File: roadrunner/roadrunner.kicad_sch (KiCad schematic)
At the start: 48 parts, among them J1 Battery_conn, J2 battery_conn_r, SW1 SW_Push, SW10 SW_Push, SW10_r1 SW_Push, SW11 SW_Push, SW11_r1 SW_Push, SW12 SW_Push, SW12_r1 SW_Push, SW13 SW_Push, SW13_r1 SW_Push, SW14 SW_Push, SW14_r1 SW_Push, SW15 SW_Push, SW15_r1 SW_Push, SW16 SW_Push, SW16_r1 SW_Push, SW17 SW_Push, SW17_r1 SW_Push, SW1_r1 SW_Push, SW2 SW_Push, SW2_r1 SW_Push, SW3 SW_Push, SW3_r1 SW_Push, SW4 SW_Push, SW4_r1 SW_Push, SW5 SW_Push, SW5_r1 SW_Push, SW6 SW_Push, SW6_r1 SW_Push, SW7 SW_Push, SW7_r1 SW_Push, SW8 SW_Push, SW8_r1 SW_Push, SW9 SW_Push, SW9_r1 SW_Push, U1 ProMicro-kbd, U2 ProMicro-kbd

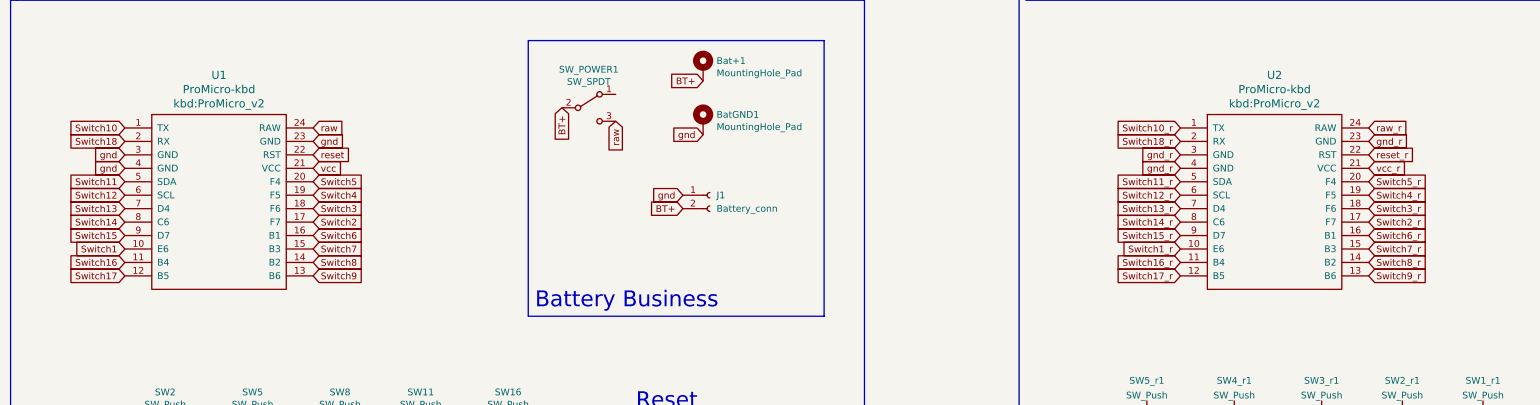
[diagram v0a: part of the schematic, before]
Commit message: update schematic
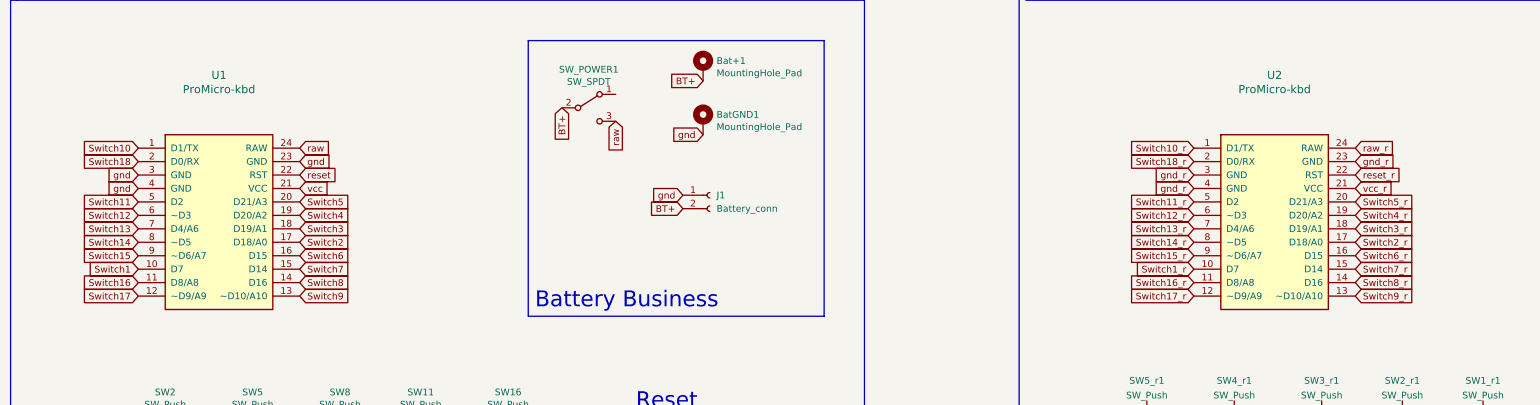
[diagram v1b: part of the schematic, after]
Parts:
- U1, U2: footprint kbd:ProMicro_v2 -> Arduino:Sparkfun_Pro_Micro; symbol sweepv2-rescue:ProMicro-kbd-bigblackpill-34key-rescue -> Arduino:Sparkfun_Pro_Micro

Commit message: update shape
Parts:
- TRRS1, TRRS2: footprint (none) -> Connector_Audio:Jack_3.5mm_PJ320E_Horizontal
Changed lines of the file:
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@@
   (symbol (lib_id "Connector:AudioJack4") (at 331.47 133.35 0) (unit 1)
     (in_bom yes) (on_board yes) (fields_autoplaced)
-    (property "Reference" "TRRS2" (id 0) (at 328.93 125.5735 0))
-    (property "Value" "AudioJack4" (id 1) (at 328.93 128.3486 0))
-    (property "Footprint" "" (id 2) (at 331.47 133.35 0)
+    (property "Reference" "TRRS2" (id 0) (at 328.93 124.46 0))
+    (property "Value" "AudioJack4" (id 1) (at 328.93 127 0))
+    (property "Footprint" "Connector_Audio:Jack_3.5mm_PJ320E_Horizontal" (id 2) (at 331.47 133.35 0)
       (effects (font (size 1.27 1.27)) hide)
     )
@@
   (symbol (lib_id "Connector:AudioJack4") (at 135.89 129.54 0) (unit 1)
     (in_bom yes) (on_board yes) (fields_autoplaced)
-    (property "Reference" "TRRS1" (id 0) (at 133.35 121.7635 0))
-    (property "Value" "AudioJack4" (id 1) (at 133.35 124.5386 0))
-    (property "Footprint" "" (id 2) (at 135.89 129.54 0)
+    (property "Reference" "TRRS1" (id 0) (at 133.35 120.65 0))
+    (property "Value" "AudioJack4" (id 1) (at 133.35 123.19 0))
+    (property "Footprint" "Connector_Audio:Jack_3.5mm_PJ320E_Horizontal" (id 2) (at 135.89 129.54 0)
       (effects (font (size 1.27 1.27)) hide)
     )
@@
   )
   (symbol (lib_id "Switch:SW_SPDT") (at 121.92 34.29 0) (unit 1)
-    (in_bom yes) (on_board yes)
-    (property "Reference" "SW_POWER1" (id 0) (at 121.92 27.051 0))
-    (property "Value" "SW_SPDT" (id 1) (at 121.92 29.3624 0))
+    (in_bom yes) (on_board yes) (fields_autoplaced)
+    (property "Reference" "SW_POWER1" (id 0) (at 121.92 26.67 0))
+    (property "Value" "SW_SPDT" (id 1) (at 121.92 29.21 0))
     (property "Footprint" "battery_switch:SPDT_C128955" (id 2) (at 121.92 34.29 0)
       (effects (font (size 1.27 1.27)) hide)
@@
   )
   (symbol (lib_id "Switch:SW_SPDT") (at 317.5 31.75 0) (unit 1)
-    (in_bom yes) (on_board yes)
-    (property "Reference" "SW_POWERR1" (id 0) (at 317.5 24.511 0))
-    (property "Value" "SW_SPDT" (id 1) (at 317.5 26.8224 0))
+    (in_bom yes) (on_board yes) (fields_autoplaced)
+    (property "Reference" "SW_POWERR1" (id 0) (at 317.5 24.13 0))
+    (property "Value" "SW_SPDT" (id 1) (at 317.5 26.67 0))
     (property "Footprint" "battery_switch:SPDT_C128955" (id 2) (at 317.5 31.75 0)
       (effects (font (size 1.27 1.27)) hide)
@@
     )
     (path "/5707fb00-48c3-46d9-8f62-42ff2e9ad9f5"
-      (reference "TRRS1") (unit 1) (value "AudioJack4") (footprint "")
+      (reference "TRRS1") (unit 1) (value "AudioJack4") (footprint "Connector_Audio:Jack_3.5mm_PJ320E_Horizontal")
     )
     (path "/5340d998-a6ef-44fa-806e-718c814691ee"
-      (reference "TRRS2") (unit 1) (value "AudioJack4") (footprint "")
+      (reference "TRRS2") (unit 1) (value "AudioJack4") (footprint "Connector_Audio:Jack_3.5mm_PJ320E_Horizontal")
     )
     (path "/6801880a-11a2-4a6a-9688-e81ed1f59985"

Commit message: basic v2 designs
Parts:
- removed TRRS1, TRRS2: AudioJack4, Connector_Audio:Jack_3.5mm_PJ320E_Horizontal, symbol Connector:AudioJack4
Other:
- note removed: "Useless TRRS"
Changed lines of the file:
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@@
-    (effects (font (size 2.9972 2.9972)) (justify left bottom))
-  )
-  (text "Useless TRRS\n" (at 321.31 121.92 0)
     (effects (font (size 2.9972 2.9972)) (justify left bottom))
   )
@@
     (effects (font (size 2.9972 2.9972)) (justify left bottom))
   )
-  (text "Useless TRRS\n" (at 123.19 118.11 0)
-    (effects (font (size 2.9972 2.9972)) (justify left bottom))
-  )
   (text "Battery Business" (at 308.61 74.93 0)
     (effects (font (size 2.9972 2.9972)) (justify left bottom))
@@
     )
   )
-  (global_label "vcc_r" (shape input) (at 336.55 133.35 0) (fields_autoplaced)
-    (effects (font (size 1.27 1.27)) (justify left))
-    (property "Intersheet References" "${INTERSHEET_REFS}" (id 0) (at 343.7728 133.2706 0)
-      (effects (font (size 1.27 1.27)) (justify left) hide)
-    )
-  )
   (global_label "gnd" (shape input) (at 80.01 95.25 270) (fields_autoplaced)
     (effects (font (size 1.27 1.27)) (justify right))
     (property "Intersheet References" "${INTERSHEET_REFS}" (id 0) (at 13.97 66.04 0)
-      (effects (font (size 1.27 1.27)) hide)
-    )
-  )
-  (global_label "gnd" (shape input) (at 140.97 134.62 0) (fields_autoplaced)
-    (effects (font (size 1.27 1.27)) (justify left))
-    (property "Intersheet References" "${INTERSHEET_REFS}" (id 0) (at 13.97 67.31 0)
       (effects (font (size 1.27 1.27)) hide)
     )
@@
     )
   )
-  (global_label "gnd" (shape input) (at 140.97 127 0) (fields_autoplaced)
-    (effects (font (size 1.27 1.27)) (justify left))
-    (property "Intersheet References" "${INTERSHEET_REFS}" (id 0) (at 13.97 59.69 0)
-      (effects (font (size 1.27 1.27)) hide)
-    )
-  )
   (global_label "Switch5" (shape input) (at 101.6 95.25 270) (fields_autoplaced)
     (effects (font (size 1.27 1.27)) (justify right))
@@
     (property "Intersheet References" "${INTERSHEET_REFS}" (id 0) (at 13.97 66.04 0)
       (effects (font (size 1.27 1.27)) hide)
-    )
-  )
-  (global_label "gnd_r" (shape input) (at 336.55 130.81 0) (fields_autoplaced)
-    (effects (font (size 1.27 1.27)) (justify left))
-    (property "Intersheet References" "${INTERSHEET_REFS}" (id 0) (at 344.0752 130.8894 0)
-      (effects (font (size 1.27 1.27)) (justify left) hide)
     )
   )
@@
     )
   )
-  (global_label "gnd_r" (shape input) (at 336.55 138.43 0) (fields_autoplaced)
-    (effects (font (size 1.27 1.27)) (justify left))
-    (property "Intersheet References" "${INTERSHEET_REFS}" (id 0) (at 344.0752 138.5094 0)
-      (effects (font (size 1.27 1.27)) (justify left) hide)
-    )
-  )
   (global_label "raw" (shape input) (at 127 36.83 270) (fields_autoplaced)
     (effects (font (size 1.27 1.27)) (justify right))
@@
     )
   )
-  (global_label "Switch18" (shape input) (at 140.97 132.08 0) (fields_autoplaced)
-    (effects (font (size 1.27 1.27)) (justify left))
-    (property "Intersheet References" "${INTERSHEET_REFS}" (id 0) (at 13.97 67.31 0)
-      (effects (font (size 1.27 1.27)) hide)
-    )
-  )
   (global_label "reset_r" (shape input) (at 336.55 110.49 0) (fields_autoplaced)
     (effects (font (size 1.27 1.27)) (justify left))
@@
     )
   )
-  (global_label "vcc" (shape input) (at 140.97 129.54 0) (fields_autoplaced)
-    (effects (font (size 1.27 1.27)) (justify left))
-    (property "Intersheet References" "${INTERSHEET_REFS}" (id 0) (at 13.97 59.69 0)
-      (effects (font (size 1.27 1.27)) hide)
-    )
-  )
   (global_label "gnd_r" (shape input) (at 265.43 92.71 270) (fields_autoplaced)
     (effects (font (size 1.27 1.27)) (justify right))
@@
     (property "Intersheet References" "${INTERSHEET_REFS}" (id 0) (at 285.6706 104.1056 90)
       (effects (font (size 1.27 1.27)) (justify right) hide)
-    )
-  )
-  (global_label "Switch18_r" (shape input) (at 336.55 135.89 0) (fields_autoplaced)
-    (effects (font (size 1.27 1.27)) (justify left))
-    (property "Intersheet References" "${INTERSHEET_REFS}" (id 0) (at 208.28 -27.94 0)
-      (effects (font (size 1.27 1.27)) hide)
     )
   )
@@
     (pin "2")
   )
-  (symbol (lib_id "Connector:AudioJack4") (at 331.47 133.35 0) (unit 1)
-    (in_bom yes) (on_board yes) (fields_autoplaced)
-    (property "Reference" "TRRS2" (id 0) (at 328.93 124.46 0))
-    (property "Value" "AudioJack4" (id 1) (at 328.93 127 0))
-    (property "Footprint" "Connector_Audio:Jack_3.5mm_PJ320E_Horizontal" (id 2) (at 331.47 133.35 0)
-      (effects (font (size 1.27 1.27)) hide)
-    )
-    (property "Datasheet" "~" (id 3) (at 331.47 133.35 0)
-      (effects (font (size 1.27 1.27)) hide)
-    )
-    (pin "R1")
-    (pin "R2")
-    (pin "S")
-    (pin "T")
-  )
-  (symbol (lib_id "Connector:AudioJack4") (at 135.89 129.54 0) (unit 1)
-    (in_bom yes) (on_board yes) (fields_autoplaced)
-    (property "Reference" "TRRS1" (id 0) (at 133.35 120.65 0))
-    (property "Value" "AudioJack4" (id 1) (at 133.35 123.19 0))
-    (property "Footprint" "Connector_Audio:Jack_3.5mm_PJ320E_Horizontal" (id 2) (at 135.89 129.54 0)
-      (effects (font (size 1.27 1.27)) hide)
-    )
-    (property "Datasheet" "~" (id 3) (at 135.89 129.54 0)
-      (effects (font (size 1.27 1.27)) hide)
-    )
-    (pin "R1")
-    (pin "R2")
-    (pin "S")
-    (pin "T")
-  )
   (symbol (lib_id "Connector:Conn_01x02_Female") (at 332.74 49.53 0) (unit 1)
     (in_bom yes) (on_board yes) (fields_autoplaced)
@@
       (reference "SW_POWERR1") (unit 1) (value "SW_SPDT") (footprint "battery_switch:SPDT_C128955")
     )
-    (path "/5707fb00-48c3-46d9-8f62-42ff2e9ad9f5"
-      (reference "TRRS1") (unit 1) (value "AudioJack4") (footprint "Connector_Audio:Jack_3.5mm_PJ320E_Horizontal")
-    )
-    (path "/5340d998-a6ef-44fa-806e-718c814691ee"
-      (reference "TRRS2") (unit 1) (value "AudioJack4") (footprint "Connector_Audio:Jack_3.5mm_PJ320E_Horizontal")
-    )
     (path "/6801880a-11a2-4a6a-9688-e81ed1f59985"

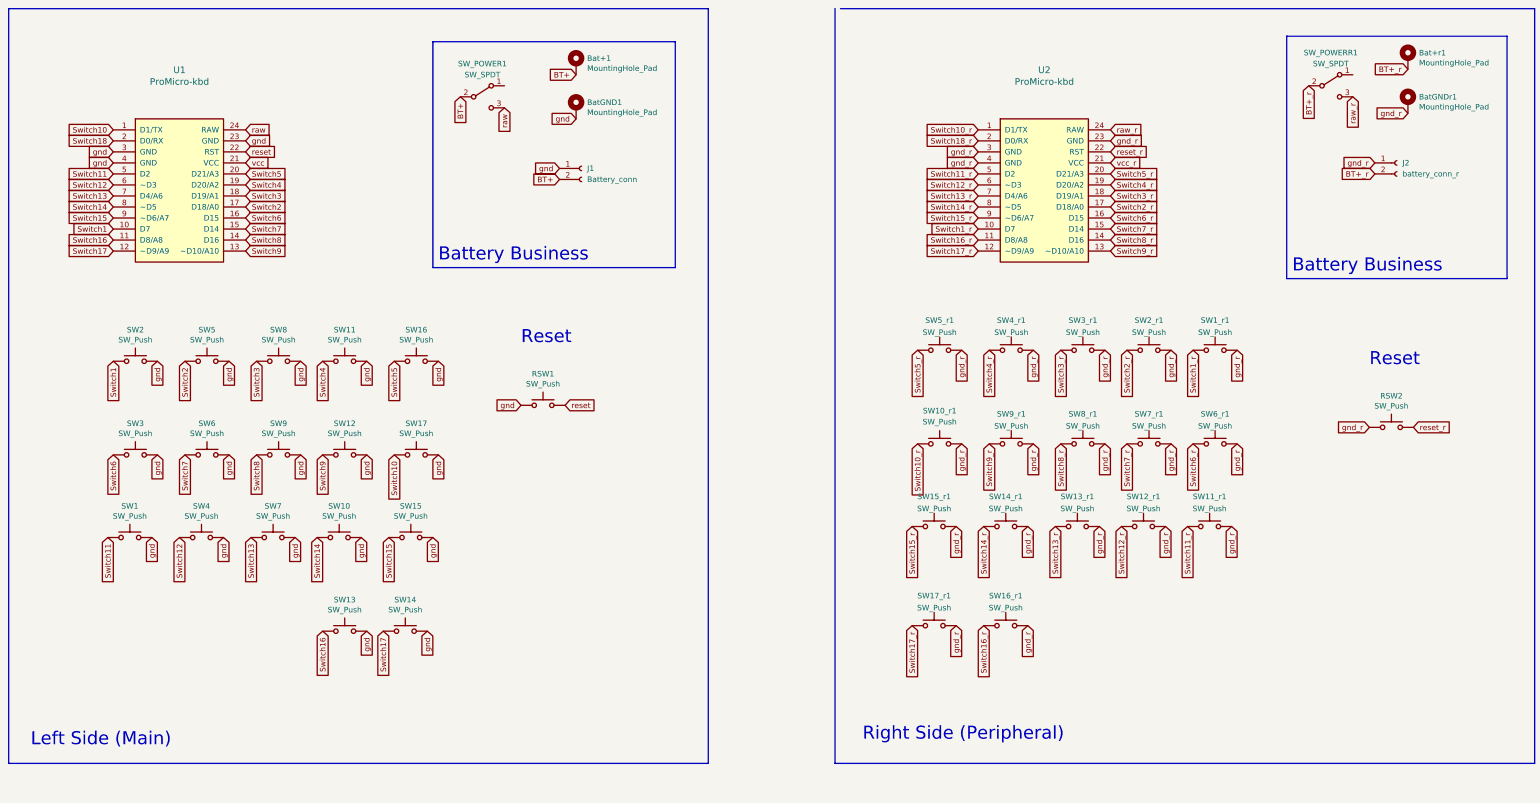
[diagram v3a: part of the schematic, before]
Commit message: begin adding diodes
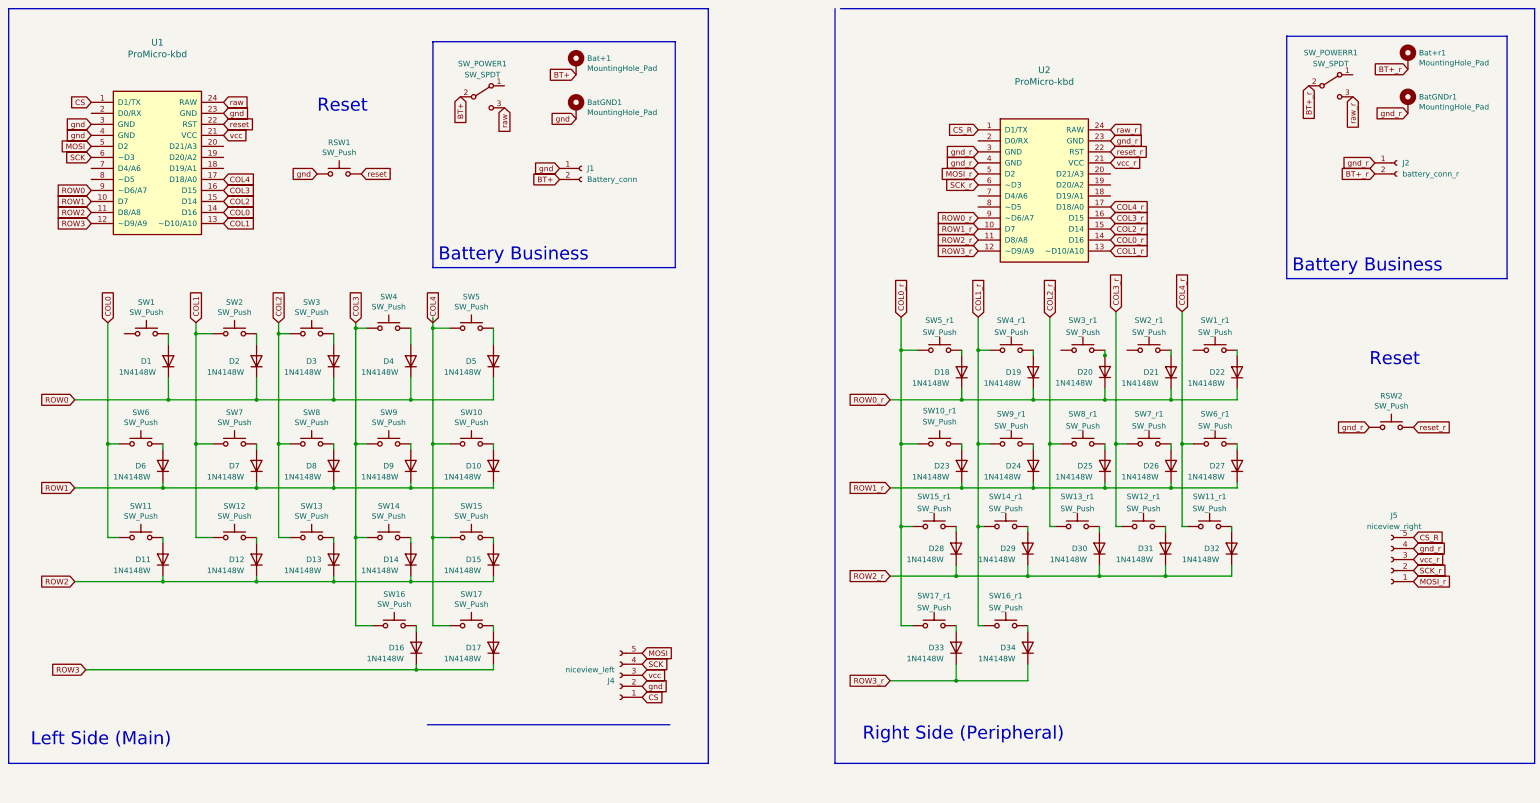
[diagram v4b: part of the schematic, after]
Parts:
- added D1, D10, D11, D12, D13, D14, D15, D16, D17, D18, D19, D2, D20, D21, D22, D23, D24, D25, D26, D27, D28, D29, D3, D30, D31, D32, D33, D34, D4, D5, D6, D7, D8, D9: 1N4148W, Diode_SMD:D_SOD-123, symbol Diode:1N4148W
- added J4: niceview_left, Connector_PinHeader_2.54mm:PinHeader_1x05_P2.54mm_Vertical, symbol Connector:Conn_01x05_Female
- added J5: niceview_right, Connector_PinHeader_2.54mm:PinHeader_1x05_P2.54mm_Vertical, symbol Connector:Conn_01x05_Female
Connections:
- net Switch2 is gone; now on net COL4: SW5.1, U1.17 (D18/A0)
- net Switch9 is gone; now on net COL1: SW12.1, U1.13 (~D10/A10)
- net Switch9_r is gone; now on net COL1_r: SW9_r1.1, U2.13 (~D10/A10)
- net gnd: now also J4.2 (Pin_2); no longer SW1.2, SW10.2, SW11.2, SW12.2, SW13.2, SW14.2, SW15.2, SW16.2, SW17.2, SW2.2, SW3.2, SW4.2, SW5.2, SW6.2, SW7.2, SW8.2, SW9.2
- net gnd_r: now also J5.4 (Pin_4); no longer SW10_r1.2, SW11_r1.2, SW12_r1.2, SW13_r1.2, SW14_r1.2, SW15_r1.2, SW16_r1.2, SW17_r1.2, SW1_r1.2, SW2_r1.2, SW3_r1.2, SW4_r1.2, SW5_r1.2, SW6_r1.2, SW7_r1.2, SW8_r1.2, SW9_r1.2
- net vcc: now also J4.3 (Pin_3)
- net vcc_r: now also J5.3 (Pin_3)
- net Switch1 renamed COL1
- net COL1: now also SW7.1; no longer U1.10 (D7)
- net Switch10 renamed COL4
- net COL4: now also SW10.1, SW15.1; no longer U1.1 (D1/TX)
- net Switch10_r renamed COL0_r
- net COL0_r: now also SW15_r1.1, SW17_r1.1, SW5_r1.1, U2.14 (D16); no longer U2.1 (D1/TX)
- net Switch11: no longer names the net of SW1.1
- net Switch11: no longer U1.5 (D2)
- net Switch11_r renamed COL4_r
- net COL4_r: now also SW6_r1.1, U2.17 (D18/A0); no longer U2.5 (D2)
- net Switch12 renamed COL3
- net COL3: now also SW14.1, SW16.1, SW9.1, U1.16 (D15); no longer U1.6 (~D3)
- net Switch12_r renamed COL3_r
- net COL3_r: now also SW7_r1.1, U2.16 (D15); no longer U2.6 (~D3)
- net Switch13: no longer names the net of U1.7 (D4/A6)
- net Switch13: no longer SW7.1
- net Switch13_r: no longer names the net of U2.7 (D4/A6)
- net Switch13_r: no longer SW13_r1.1
- net Switch14: no longer names the net of U1.8 (~D5)
- net Switch14: no longer SW10.1
- net Switch14_r: no longer names the net of U2.8 (~D5)
- net Switch14_r: no longer SW14_r1.1
- net Switch15 renamed ROW0
- net ROW0: now also D1.1 (K), D2.1 (K), D3.1 (K), D4.1 (K), D5.1 (K); no longer SW15.1
- net Switch15_r renamed ROW0_r
- net ROW0_r: now also D18.1 (K), D19.1 (K), D21.1 (K), D22.1 (K); no longer SW15_r1.1
- net Switch16 renamed COL2
- net COL2: now also SW3.1, SW8.1, U1.15 (D14); no longer U1.11 (D8/A8)
- net Switch16_r renamed COL1_r
- net COL1_r: now also SW14_r1.1, SW4_r1.1; no longer U2.11 (D8/A8)
- net Switch17 renamed ROW3
- net ROW3: now also D16.1 (K), D17.1 (K); no longer SW14.1
- net Switch17_r renamed ROW3_r
- net ROW3_r: now also D33.1 (K), D34.1 (K); no longer SW17_r1.1
- net Switch18: no longer names the net of U1.2 (D0/RX)
- net Switch18_r: no longer names the net of U2.2 (D0/RX)
- net Switch1_r: no longer names the net of SW1_r1.1
- net Switch1_r: no longer U2.10 (D7)
- net Switch2_r: no longer names the net of SW2_r1.1
- net Switch2_r: no longer U2.17 (D18/A0)
- net Switch3: no longer names the net of U1.18 (D19/A1)
- net Switch3: no longer SW8.1
- net Switch3_r: no longer names the net of U2.18 (D19/A1)
- net Switch3_r: no longer SW3_r1.1
- net Switch4: no longer names the net of U1.19 (D20/A2)
- net Switch4: no longer SW11.1
- net Switch4_r: no longer names the net of U2.19 (D20/A2)
- net Switch4_r: no longer SW4_r1.1
- net Switch5: no longer names the net of U1.20 (D21/A3)
- net Switch5: no longer SW16.1
- net Switch5_r: no longer names the net of U2.20 (D21/A3)
- net Switch5_r: no longer SW5_r1.1
- removed net Switch6: SW3.1, U1.16 (D15)
- removed net Switch6_r: SW6_r1.1, U2.16 (D15)
- net Switch7 renamed COL0
- net COL0: now also SW11.1, U1.14 (D16); no longer U1.15 (D14)
- net Switch7_r renamed COL2_r
- net COL2_r: now also SW13_r1.1, SW8_r1.1; no longer SW7_r1.1
- removed net Switch8: SW9.1, U1.14 (D16)
- removed net Switch8_r: SW8_r1.1, U2.14 (D16)
- new net: D9.2 (A), SW9.2
- new net: D2.2 (A), SW2.2
- new net: D32.2 (A), SW11_r1.2
- new net: D4.2 (A), SW4.2
- new net: D13.2 (A), SW13.2
- new net: D20.2 (A), SW3_r1.2
- new net: D34.2 (A), SW16_r1.2
- new net: D23.2 (A), SW10_r1.2
- new net: D11.2 (A), SW11.2
- new net: D18.2 (A), SW5_r1.2
- new net: D26.2 (A), SW7_r1.2
- new net: D19.2 (A), SW4_r1.2
- new net: D28.2 (A), SW15_r1.2
- new net: D16.2 (A), SW16.2
- new net: D31.2 (A), SW12_r1.2
- new net: D33.2 (A), SW17_r1.2
- new net: D8.2 (A), SW8.2
- new net: D6.2 (A), SW6.2
- new net: D29.2 (A), SW14_r1.2
- new net: D15.2 (A), SW15.2
- new net: D1.2 (A), SW1.2
- new net: D3.2 (A), SW3.2
- new net: D14.2 (A), SW14.2
- new net: D5.2 (A), SW5.2
- new net: D10.2 (A), SW10.2
- new net: D22.2 (A), SW1_r1.2
- new net: D17.2 (A), SW17.2
- new net: D12.2 (A), SW12.2
- new net: D24.2 (A), SW9_r1.2
- new net: D21.2 (A), SW2_r1.2
- new net: D27.2 (A), SW6_r1.2
- new net: D7.2 (A), SW7.2
- new net: D30.2 (A), SW13_r1.2
- new net: D25.2 (A), SW8_r1.2
- new net CS: J4.1 (Pin_1), U1.1 (D1/TX)
- new net CS_R: J5.5 (Pin_5), U2.1 (D1/TX)
- new net MOSI: J4.5 (Pin_5), U1.5 (D2)
- new net MOSI_r: J5.1 (Pin_1), U2.5 (D2)
- new net ROW1: D10.1 (K), D6.1 (K), D7.1 (K), D8.1 (K), D9.1 (K), U1.10 (D7)
- new net ROW1_r: D23.1 (K), D24.1 (K), D25.1 (K), D26.1 (K), D27.1 (K), U2.10 (D7)
- new net ROW2: D11.1 (K), D12.1 (K), D13.1 (K), D14.1 (K), D15.1 (K), U1.11 (D8/A8)
- new net ROW2_r: D28.1 (K), D29.1 (K), D30.1 (K), D31.1 (K), D32.1 (K), U2.11 (D8/A8)
- new net SCK: J4.4 (Pin_4), U1.6 (~D3)
- new net SCK_r: J5.2 (Pin_2), U2.6 (~D3)
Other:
- moved on the sheet: RSW1, SW1, SW10, SW11, SW12, SW13, SW14, SW15, SW16, SW17, SW2, SW3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
